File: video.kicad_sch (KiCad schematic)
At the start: 74 parts, among them Q10 2N3906, Q4 2N3906, Q5 2N3906, Q6 2N3906, Q7 2N3906, Q8 2N3906, Q9 2N3906

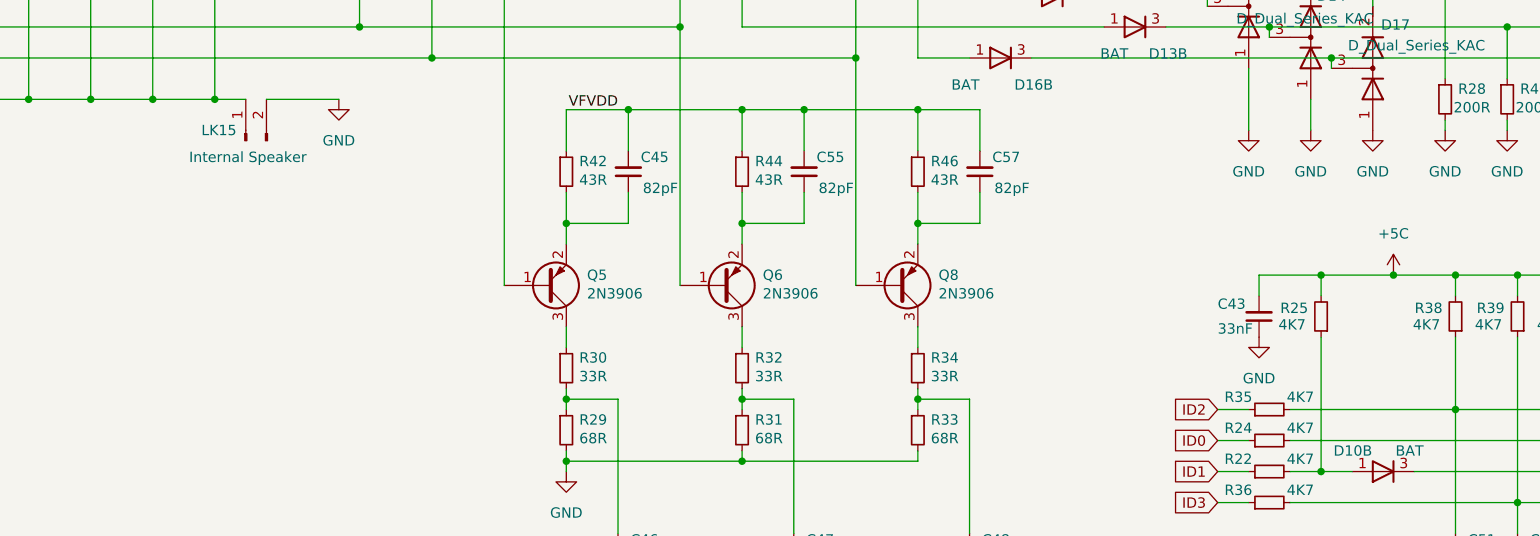
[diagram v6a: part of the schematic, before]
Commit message: add missing capacitors
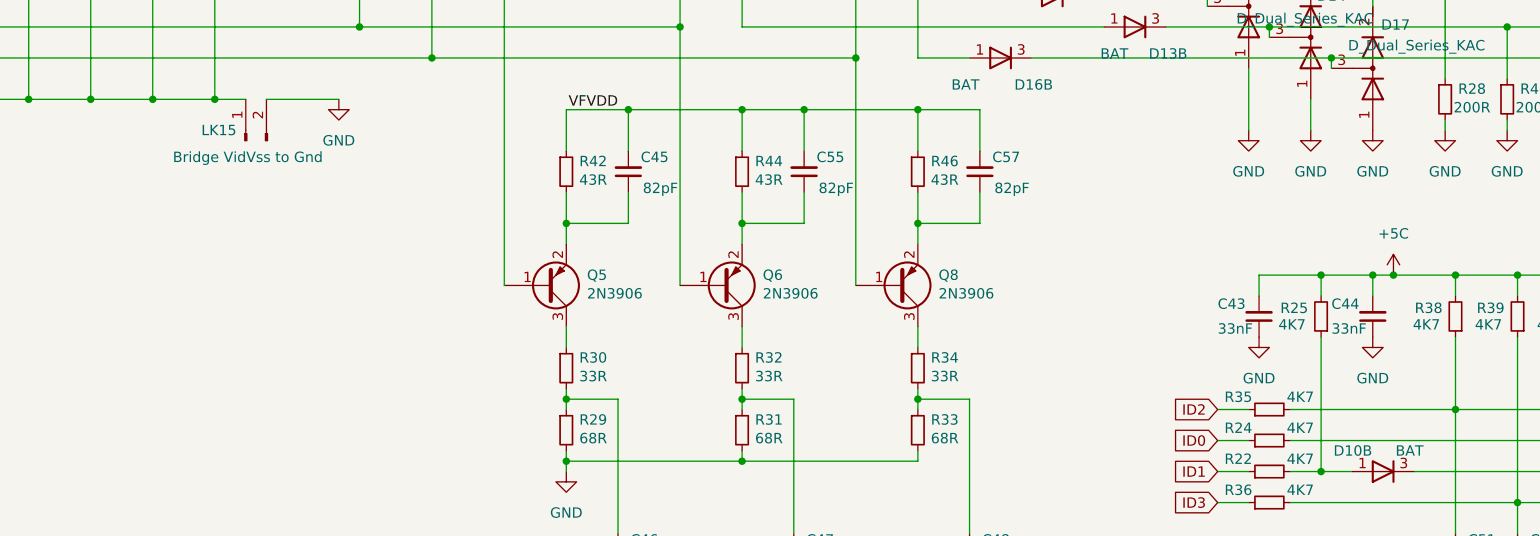
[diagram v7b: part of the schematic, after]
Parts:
- added C44: 33nF, Capacitor_SMD:C_0805_2012Metric, symbol Device:C_Small
- LK15: value Internal Speaker -> Bridge VidVss to Gnd
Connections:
- net +5C: now also C44.2
- net GND: now also C44.1
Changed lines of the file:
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@@
 	)
 	(junction
+		(at 196.85 85.09)
+		(diameter 0)
+		(color 0 0 0 0)
+	)
+	(junction
 		(at 207.01 85.09)
 		(diameter 0)
@@
 	(wire
 		(pts
-			(xy 190.5 85.09) (xy 199.39 85.09)
+			(xy 190.5 85.09) (xy 196.85 85.09)
 		)
 		(stroke
@@
 	(wire
 		(pts
+			(xy 196.85 85.09) (xy 196.85 87.63)
+		)
+		(stroke
+			(width 0)
+			(type default)
+		)
+	)
+	(wire
+		(pts
 			(xy 191.77 59.69) (xy 191.77 58.42)
 		)
@@
 	(wire
 		(pts
+			(xy 196.85 85.09) (xy 199.39 85.09)
+		)
+		(stroke
+			(width 0)
+			(type default)
+		)
+	)
+	(wire
+		(pts
 			(xy 81.28 58.42) (xy 81.28 48.26)
 		)
@@
 	)
 	(symbol
+		(lib_id "Device:C_Small")
+		(at 196.85 90.17 180)
+		(unit 1)
+		(exclude_from_sim no)
+		(in_bom yes)
+		(on_board yes)
+		(dnp no)
+		(property "Reference" "C44"
+			(at 191.77 88.646 0)
+			(effects
+				(font
+					(size 1.27 1.27)
+				)
+				(justify right)
+			)
+		)
+		(property "Value" "33nF"
+			(at 191.77 91.694 0)
+			(effects
+				(font
+					(size 1.27 1.27)
+				)
+				(justify right)
+			)
+		)
+		(property "Footprint" "Capacitor_SMD:C_0805_2012Metric"
+			(at 196.85 90.17 0)
+			(effects
+				(font
+					(size 1.27 1.27)
+				)
+				(hide yes)
+			)
+		)
+		(property "Datasheet" "~"
+			(at 196.85 90.17 0)
+			(effects
+				(font
+					(size 1.27 1.27)
+				)
+				(hide yes)
+			)
+		)
+		(property "Description" "Unpolarized capacitor, small symbol"
+			(at 196.85 90.17 0)
+			(effects
+				(font
+					(size 1.27 1.27)
+				)
+				(hide yes)
+			)
+		)
+		(pin "1"
+		)
+		(pin "2"
+		)
+		(instances
+			(project "Acorn-A3010"
+				(path "/999882f3-94f8-4a89-9093-27a47d0cb289/21031065-42cd-49d4-b299-d2e76b62bbd8"
+					(reference "C44")
+					(unit 1)
+				)
+			)
+		)
+	)
+	(symbol
 		(lib_id "Device:D_Dual_CommonAnode_AKK_Split")
 		(at 198.12 109.22 0)
@@
 			)
 		)
-		(property "Value" "Internal Speaker"
+		(property "Value" "Bridge VidVss to Gnd"
 			(at 58.674 70.612 90)
 			(effects
@@
 					(unit 1)
 				)
+			)
+		)
+	)
+	(symbol
+		(lib_id "power:GND")
+		(at 196.85 92.71 0)
+		(unit 1)
+		(exclude_from_sim no)
+		(in_bom yes)
+		(on_board yes)
+		(dnp no)
+		(fields_autoplaced yes)
+		(property "Reference" "#PWR0265"
+			(at 196.85 99.06 0)
+			(effects
+				(font
+					(size 1.27 1.27)
+				)
+				(hide yes)
+			)
+		)
+		(property "Value" "GND"
+			(at 196.85 97.79 0)
+			(effects
+				(font
+					(size 1.27 1.27)
+				)
+			)
+		)
+		(property "Footprint" ""
+			(at 196.85 92.71 0)
+			(effects
+				(font
+					(size 1.27 1.27)
+				)
+				(hide yes)
+			)
+		)
+		(property "Datasheet" ""
+			(at 196.85 92.71 0)
+			(effects
+				(font
+					(size 1.27 1.27)
+				)
+				(hide yes)
+			)
+		)
+		(property "Description" "Power symbol creates a global label with name \"GND\" , ground"
+			(at 196.85 92.71 0)
+			(effects
+				(font
+					(size 1.27 1.27)
+				)
+				(hide yes)
+			)
+		)
+		(pin "1"
+		)
+		(instances
+			(project "Acorn-A3010"
+				(path "/999882f3-94f8-4a89-9093-27a47d0cb289/21031065-42cd-49d4-b299-d2e76b62bbd8"
+					(reference "#PWR0265")
+					(unit 1)
+				)

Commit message: fix footprint sizes
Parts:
- R57, R58, R59: footprint Resistor_SMD:R_0805_2012Metric -> Resistor_SMD:R_1206_3216Metric
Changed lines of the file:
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@@
 			)
 		)
-		(property "Footprint" "Resistor_SMD:R_0805_2012Metric"
+		(property "Footprint" "Resistor_SMD:R_1206_3216Metric"
 			(at 72.39 45.72 0)
 			(effects
@@
 			)
 		)
-		(property "Footprint" "Resistor_SMD:R_0805_2012Metric"
+		(property "Footprint" "Resistor_SMD:R_1206_3216Metric"
 			(at 63.5 45.72 0)
 			(effects
@@
 			)
 		)
-		(property "Footprint" "Resistor_SMD:R_0805_2012Metric"
+		(property "Footprint" "Resistor_SMD:R_1206_3216Metric"
 			(at 81.28 45.72 0)
 			(effects
